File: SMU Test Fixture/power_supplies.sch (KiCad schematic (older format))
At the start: 111 parts, among them J13 Conn_WallSocket_Earth, Q1 Si2347DS, Q10 BC857, Q2 Si2347DS, Q3 BCP56, Q4 Si2347DS, Q5 Si2347DS, Q6 NJVMJB42CT4G, Q7 BCP56, Q8 BCP56, Q9 BCP56, T1 VPP12-4400, T2 VPP36-820, U10 MIC29510-5.0WT, U11 LT3045xMSE-1, U12 LT3094xMSE, U9 LM393

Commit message: Add footprints for low precision/low power parts.
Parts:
- C32, C33: footprint (none) -> Capacitor_SMD:C_0805_2012Metric_Pad1.18x1.45mm_HandSolder
- R31, R32, R33, R34, R35, R36, R37, R38, R39, R40, R66, R67, R68: footprint (none) -> Resistor_SMD:R_0805_2012Metric_Pad1.20x1.40mm_HandSolder
- T1: footprint XFMR_VPP12-4400 -> eaton:XFMR_VPP12-4400
- T2: footprint XFMR_VPP36-820 -> eaton:XFMR_VPP36-820
- U9: footprint (none) -> Package_SO:TSSOP-8_4.4x3mm_P0.65mm
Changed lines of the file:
@@
 F 0 "R66" H 9693 1946 50  0000 L CNN
 F 1 "150k" H 9650 1825 50  0000 L CNN
-F 2 "" H 9625 1900 50  0001 C CNN
+F 2 "Resistor_SMD:R_0805_2012Metric_Pad1.20x1.40mm_HandSolder" H 9625 1900 50  0001 C CNN
 F 3 "~" H 9625 1900 50  0001 C CNN
 	1    9625 1900
@@
 F 0 "R67" H 9693 2546 50  0000 L CNN
 F 1 "150k" H 9650 2425 50  0000 L CNN
-F 2 "" H 9625 2500 50  0001 C CNN
+F 2 "Resistor_SMD:R_0805_2012Metric_Pad1.20x1.40mm_HandSolder" H 9625 2500 50  0001 C CNN
 F 3 "~" H 9625 2500 50  0001 C CNN
 	1    9625 2500
@@
 F 0 "T1" H 2275 6250 50  0000 C CNN
 F 1 "VPP12-4400" H 2275 6150 50  0000 C CNN
-F 2 "XFMR_VPP12-4400" H 2275 5525 50  0001 C CNN
+F 2 "eaton:XFMR_VPP12-4400" H 2275 5525 50  0001 C CNN
 F 3 "https://www.mouser.com/datasheet/2/410/VPP12_4400-781393.pdf" H 2275 5525 50  0001 C CNN
 F 4 "VPP12-4400" H 2275 5525 50  0001 C CNN "PN"
@@
 F 0 "T2" H 5325 2781 50  0000 C CNN
 F 1 "VPP36-820" H 5325 2850 50  0000 C CNN
-F 2 "XFMR_VPP36-820" H 5325 2200 50  0001 C CNN
+F 2 "eaton:XFMR_VPP36-820" H 5325 2200 50  0001 C CNN
 F 3 "https://www.mouser.com/datasheet/2/410/VPP36_820-781788.pdf" H 5325 2200 50  0001 C CNN
 F 4 "VPP36-820" H 5325 2200 50  0001 C CNN "PN"
@@
 F 0 "U9" H 1925 2300 50  0000 C CNN
 F 1 "LM393" H 1875 2225 50  0000 C CNN
-F 2 "" H 1900 2450 50  0001 C CNN
+F 2 "Package_SO:TSSOP-8_4.4x3mm_P0.65mm" H 1900 2450 50  0001 C CNN
 F 3 "http://www.ti.com/lit/ds/symlink/lm393.pdf" H 1900 2450 50  0001 C CNN
 	1    1900 2450
@@
 F 0 "U9" H 1875 3500 50  0000 C CNN
 F 1 "LM393" H 1875 3400 50  0000 C CNN
-F 2 "" H 1875 3750 50  0001 C CNN
+F 2 "Package_SO:TSSOP-8_4.4x3mm_P0.65mm" H 1875 3750 50  0001 C CNN
 F 3 "http://www.ti.com/lit/ds/symlink/lm393.pdf" H 1875 3750 50  0001 C CNN
 	2    1875 3750
@@
 F 0 "R31" H 575 3550 50  0000 L CNN
 F 1 "10k" H 525 3475 50  0000 L CNN
-F 2 "" H 725 3475 50  0001 C CNN
+F 2 "Resistor_SMD:R_0805_2012Metric_Pad1.20x1.40mm_HandSolder" H 725 3475 50  0001 C CNN
 F 3 "~" H 725 3475 50  0001 C CNN
 	1    725  3475
@@
 F 0 "U9" H 1208 1171 50  0000 L CNN
 F 1 "LM393" H 1208 1080 50  0000 L CNN
-F 2 "" H 1250 1125 50  0001 C CNN
+F 2 "Package_SO:TSSOP-8_4.4x3mm_P0.65mm" H 1250 1125 50  0001 C CNN
 F 3 "http://www.ti.com/lit/ds/symlink/lm393.pdf" H 1250 1125 50  0001 C CNN
 	3    1250 1125
@@
 F 0 "R32" H 575 3900 50  0000 L CNN
 F 1 "2.5k" H 500 3800 50  0000 L CNN
-F 2 "" H 725 3825 50  0001 C CNN
+F 2 "Resistor_SMD:R_0805_2012Metric_Pad1.20x1.40mm_HandSolder" H 725 3825 50  0001 C CNN
 F 3 "~" H 725 3825 50  0001 C CNN
 	1    725  3825
@@
 F 0 "C32" H 7875 1675 50  0000 L CNN
 F 1 "1n" H 7925 1600 50  0000 L CNN
-F 2 "" H 7850 1600 50  0001 C CNN
+F 2 "Capacitor_SMD:C_0805_2012Metric_Pad1.18x1.45mm_HandSolder" H 7850 1600 50  0001 C CNN
 F 3 "~" H 7850 1600 50  0001 C CNN
 	1    7850 1600
@@
 F 0 "R39" H 2293 3571 50  0000 L CNN
 F 1 "3K" H 2293 3480 50  0000 L CNN
-F 2 "" H 2225 3525 50  0001 C CNN
+F 2 "Resistor_SMD:R_0805_2012Metric_Pad1.20x1.40mm_HandSolder" H 2225 3525 50  0001 C CNN
 F 3 "~" H 2225 3525 50  0001 C CNN
 	1    2225 3525
@@
 F 0 "R35" V 1475 3850 50  0000 C CNN
 F 1 "10K" V 1550 3850 50  0000 C CNN
-F 2 "" H 1400 3850 50  0001 C CNN
+F 2 "Resistor_SMD:R_0805_2012Metric_Pad1.20x1.40mm_HandSolder" H 1400 3850 50  0001 C CNN
 F 3 "~" H 1400 3850 50  0001 C CNN
 	1    1400 3850
@@
 F 0 "R37" V 2050 4025 50  0000 C CNN
 F 1 "10M" V 1975 4025 50  0000 C CNN
-F 2 "" H 1875 4025 50  0001 C CNN
+F 2 "Resistor_SMD:R_0805_2012Metric_Pad1.20x1.40mm_HandSolder" H 1875 4025 50  0001 C CNN
 F 3 "~" H 1875 4025 50  0001 C CNN
 	1    1875 4025
@@
 F 0 "R33" H 600 2250 50  0000 L CNN
 F 1 "10k" H 550 2175 50  0000 L CNN
-F 2 "" H 750 2175 50  0001 C CNN
+F 2 "Resistor_SMD:R_0805_2012Metric_Pad1.20x1.40mm_HandSolder" H 750 2175 50  0001 C CNN
 F 3 "~" H 750 2175 50  0001 C CNN
 	1    750  2175
@@
 F 0 "R34" H 600 2600 50  0000 L CNN
 F 1 "2.5k" H 525 2500 50  0000 L CNN
-F 2 "" H 750 2525 50  0001 C CNN
+F 2 "Resistor_SMD:R_0805_2012Metric_Pad1.20x1.40mm_HandSolder" H 750 2525 50  0001 C CNN
 F 3 "~" H 750 2525 50  0001 C CNN
 	1    750  2525
@@
 F 0 "R40" H 2318 2271 50  0000 L CNN
 F 1 "3K" H 2318 2180 50  0000 L CNN
-F 2 "" H 2250 2225 50  0001 C CNN
+F 2 "Resistor_SMD:R_0805_2012Metric_Pad1.20x1.40mm_HandSolder" H 2250 2225 50  0001 C CNN
 F 3 "~" H 2250 2225 50  0001 C CNN
 	1    2250 2225
@@
 F 0 "R36" V 1500 2550 50  0000 C CNN
 F 1 "10K" V 1575 2550 50  0000 C CNN
-F 2 "" H 1425 2550 50  0001 C CNN
+F 2 "Resistor_SMD:R_0805_2012Metric_Pad1.20x1.40mm_HandSolder" H 1425 2550 50  0001 C CNN
 F 3 "~" H 1425 2550 50  0001 C CNN
 	1    1425 2550
@@
 F 0 "R38" V 2075 2725 50  0000 C CNN
 F 1 "10M" V 2000 2725 50  0000 C CNN
-F 2 "" H 1900 2725 50  0001 C CNN
+F 2 "Resistor_SMD:R_0805_2012Metric_Pad1.20x1.40mm_HandSolder" H 1900 2725 50  0001 C CNN
 F 3 "~" H 1900 2725 50  0001 C CNN
 	1    1900 2725
@@
 F 0 "C33" H 7875 2875 50  0000 L CNN
 F 1 "1n" H 7925 2800 50  0000 L CNN
-F 2 "" H 7850 2800 50  0001 C CNN
+F 2 "Capacitor_SMD:C_0805_2012Metric_Pad1.18x1.45mm_HandSolder" H 7850 2800 50  0001 C CNN
 F 3 "~" H 7850 2800 50  0001 C CNN
 	1    7850 2800
@@
 F 0 "R68" H 10343 4871 50  0000 L CNN
 F 1 "390K" H 10343 4780 50  0000 L CNN
-F 2 "" H 10275 4825 50  0001 C CNN
+F 2 "Resistor_SMD:R_0805_2012Metric_Pad1.20x1.40mm_HandSolder" H 10275 4825 50  0001 C CNN
 F 3 "~" H 10275 4825 50  0001 C CNN
 	1    10275 4825

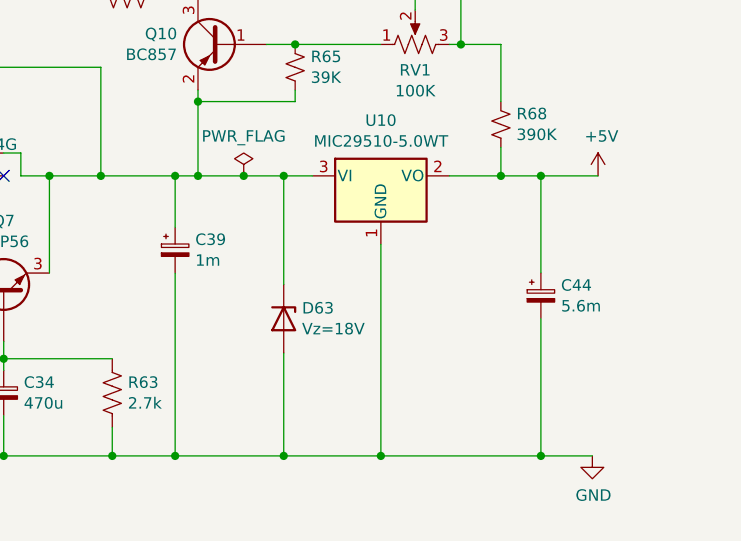
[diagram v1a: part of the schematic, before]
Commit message: More footprints added.
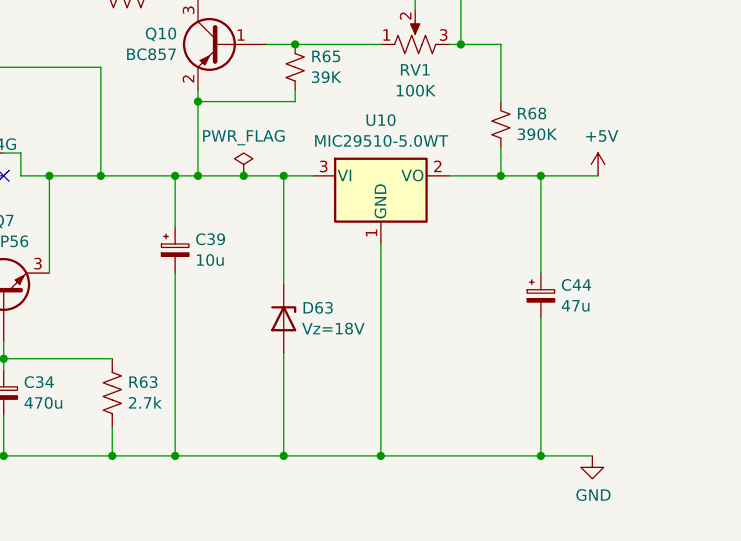
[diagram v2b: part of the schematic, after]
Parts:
- C26, C27, C28, C40, C41, C42, C43, C45, C46: footprint (none) -> Capacitor_SMD:C_0805_2012Metric_Pad1.18x1.45mm_HandSolder
- C39: value 1m -> 10u; footprint Capacitor_SMD:CP_Elec_16x22 -> Capacitor_SMD:C_Elec_5x5.8; PN UCZ1H102MNS1MS -> UUT1V100MCL1GS
- C44: value 5.6m -> 47u; footprint (none) -> Capacitor_SMD:CP_Elec_8x10; PN (none) -> UUB1V470MNL1GS
- D37, D38, D39, D40, D50, D51, D52, D53: footprint (none) -> Package_TO_SOT_SMD:TO-263-3_TabPin2; PN (none) -> VS-8ETH06-1HM3
- D41, D42, D47, D48, D49: footprint (none) -> Diode_SMD:D_SOD-123; PN (none) -> RS07D-HM3-08
- D43, D56, D57: footprint (none) -> Package_TO_SOT_SMD:SOT-323_SC-70_Handsoldering; PN (none) -> SZMMBZH15VAWT1G
- D44, D54, D55: footprint (none) -> Package_TO_SOT_SMD:SOT-323_SC-70_Handsoldering
- D45: footprint (none) -> Diode_SMD:D_SOD-323_HandSoldering; PN (none) -> MM3Z5V6B
- D46: footprint (none) -> Diode_SMD:D_SOD-123
- RV1: footprint (none) -> Potentiometer_SMD:Potentiometer_Bourns_TC33X_Vertical; PN (none) -> TC33X-2-104E

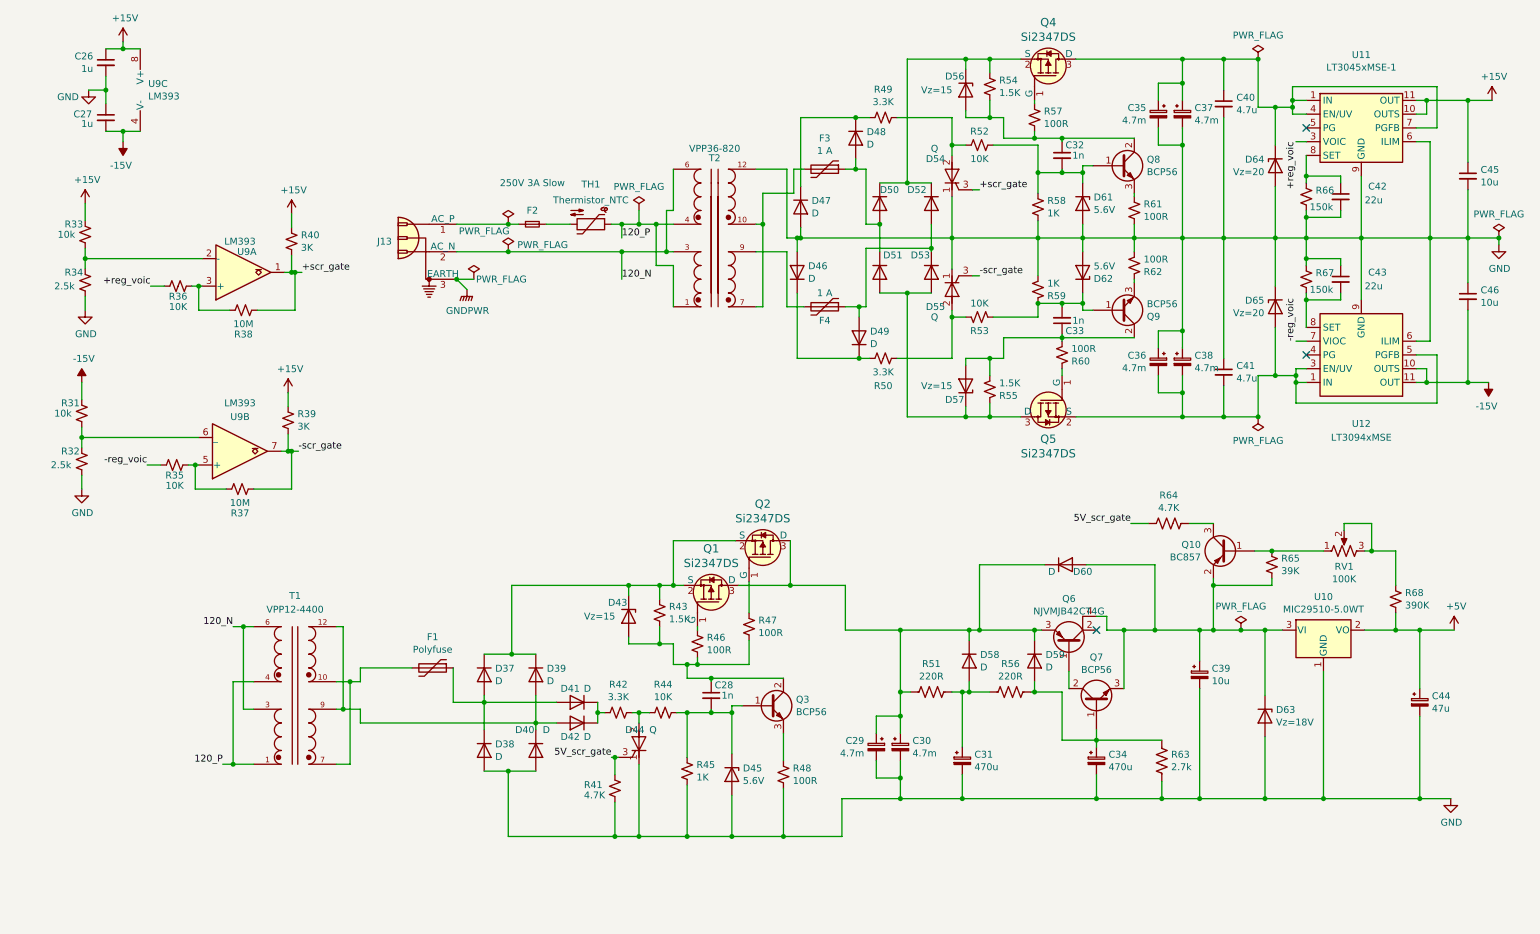
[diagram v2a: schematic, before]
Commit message: NTC calulations/specs done.
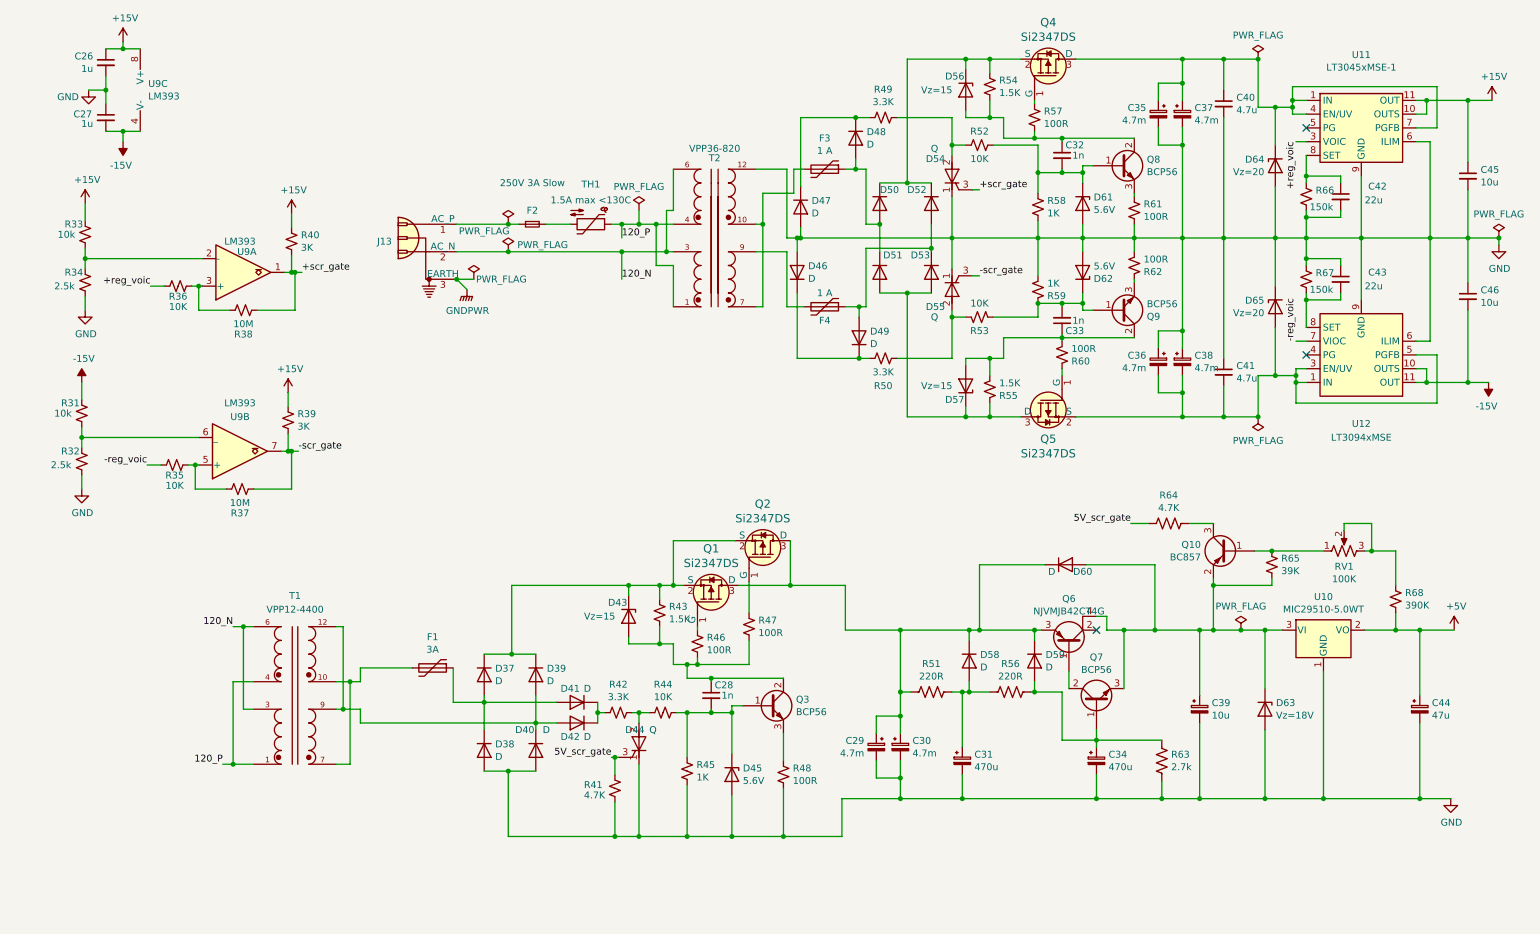
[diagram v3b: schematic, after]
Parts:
- D58, D59, D60: footprint (none) -> Diode_SMD:D_SOD-123; PN (none) -> RS07D-HM3-08
- D61, D62: footprint (none) -> Capacitor_SMD:C_0805_2012Metric_Pad1.18x1.45mm_HandSolder; PN (none) -> BZY55B5V6 RBG
- D63: footprint (none) -> Diode_SMD:D_SOD-523; PN (none) -> BZX584C18-G3-08
- D64, D65: footprint (none) -> Diode_SMD:D_SOD-523; PN (none) -> BZX584C20-G3-08
- F1: value Polyfuse -> 3A; footprint (none) -> Fuse:Fuse_1812_4532Metric_Pad1.30x3.40mm_HandSolder; PN (none) -> MF-MSMF150/24X-2
- R41, R42, R43, R44, R45, R46, R47, R48, R49, R50, R51, R52, R53, R54, R55, R56, R57, R58, R59, R60, R61, R62, R63, R64, R65: footprint (none) -> Resistor_SMD:R_0805_2012Metric_Pad1.20x1.40mm_HandSolder
- TH1: value Thermistor_NTC -> 1.5A max <130C; footprint (none) -> eaton:NTC d=11.5 p=5mm w=6mm; PN (none) -> B57236S0121M051
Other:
- moved on the sheet: C39, C44, D63

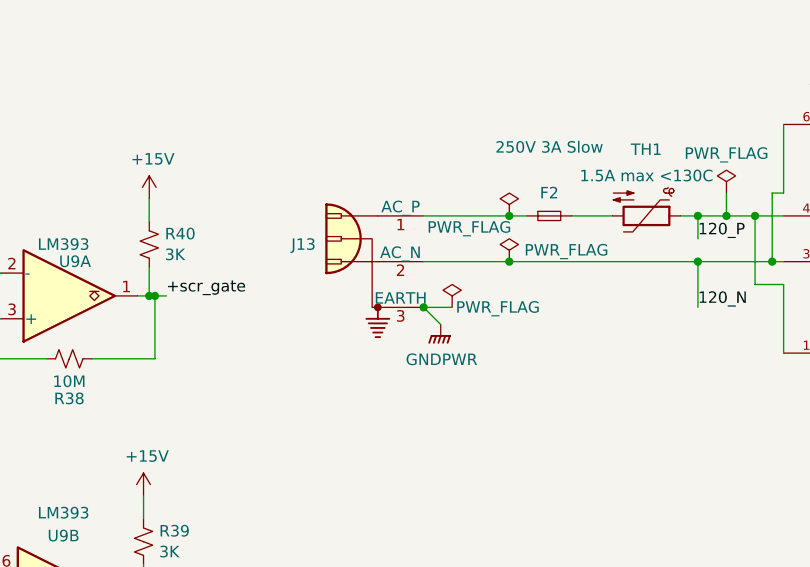
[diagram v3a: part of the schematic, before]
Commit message: Remove edison plug from schematic, now wire holes.
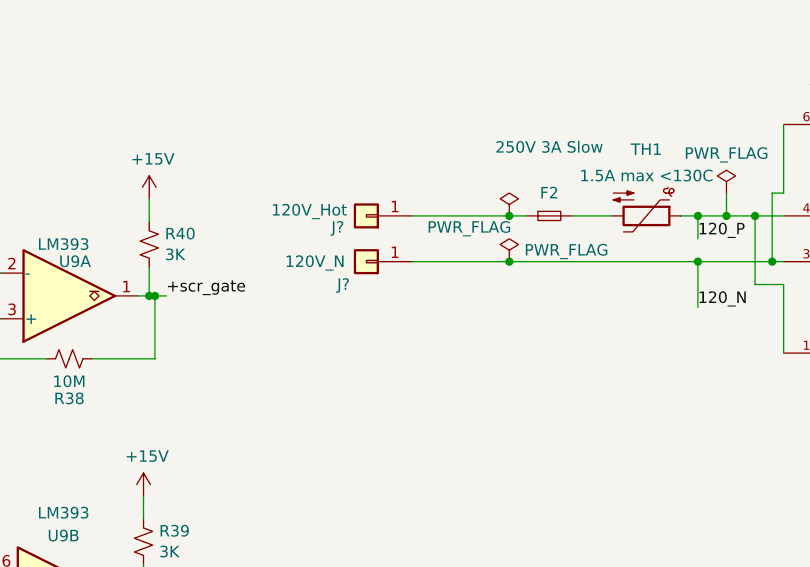
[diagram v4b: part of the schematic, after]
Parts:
- removed J13: Conn_WallSocket_Earth, symbol Connector:Conn_WallSocket_Earth
- added J?: 120V_Hot, Connector_Wire:SolderWire-0.75sqmm_1x01_D1.25mm_OD2.3mm, symbol Connector_Generic:Conn_01x01
- added J?: 120V_N, Connector_Wire:SolderWire-0.75sqmm_1x01_D1.25mm_OD2.3mm, symbol Connector_Generic:Conn_01x01
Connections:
- net 120_N: now also J?.1 (Pin_1)
- net at F2.1: now also J?.1 (Pin_1)
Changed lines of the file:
@@
-$EndComp
-$Comp
-L Connector:Conn_WallSocket_Earth J13
-U 1 1 6010B62B
-P 3250 2300
-F 0 "J13" H 3575 2375 50  0000 C CNN
-F 1 "Conn_WallSocket_Earth" H 3256 2634 50  0001 C CNN
-F 2 "" H 2950 2400 50  0001 C CNN
-F 3 "~" H 2950 2400 50  0001 C CNN
-	1    3250 2300
-	-1   0    0    -1
 $EndComp
 $Comp
@@
 $EndComp
 Wire Wire Line
-	3450 2300 3825 2300
+	3400 2300 3825 2300
 $Comp
 L power:GND #PWR074
@@
 Wire Wire Line
 	9150 5050 9325 5050
-$Comp
-L power:GNDPWR #PWR069
-U 1 1 60086BE8
-P 3525 2575
-F 0 "#PWR069" H 3525 2375 50  0001 C CNN
-F 1 "GNDPWR" H 3529 2421 50  0000 C CNN
-F 2 "" H 3525 2525 50  0001 C CNN
-F 3 "" H 3525 2525 50  0001 C CNN
-	1    3525 2575
-	1    0    0    -1
-$EndComp
-Wire Wire Line
-	3525 2575 3450 2500
-$Comp
-L power:PWR_FLAG #FLG01
-U 1 1 600A3F9C
-P 3575 2500
-F 0 "#FLG01" H 3575 2575 50  0001 C CNN
-F 1 "PWR_FLAG" H 3775 2500 50  0000 C CNN
-F 2 "" H 3575 2500 50  0001 C CNN
-F 3 "~" H 3575 2500 50  0001 C CNN
-	1    3575 2500
-	1    0    0    -1
-$EndComp
-Wire Wire Line
-	3575 2500 3450 2500
-Connection ~ 3450 2500
-Wire Wire Line
-	3450 2100 3825 2100
+Wire Wire Line
+	3400 2100 3825 2100
 $Comp
 L power:PWR_FLAG #FLG04
@@
 	0    1    1    0
 $EndComp
+$Comp
+L Connector_Generic:Conn_01x01 J?
+U 1 1 601511D3
+P 3200 2100
+F 0 "J?" H 3325 2150 50  0000 C CNN
+F 1 "120V_Hot" H 3450 2075 50  0000 C CNN
+F 2 "Connector_Wire:SolderWire-0.75sqmm_1x01_D1.25mm_OD2.3mm" H 3200 2100 50  0001 C CNN
+F 3 "~" H 3200 2100 50  0001 C CNN
+	1    3200 2100
+	-1   0    0    1
+$EndComp
+$Comp
+L Connector_Generic:Conn_01x01 J?
+U 1 1 60151E3B
+P 3200 2300
+F 0 "J?" H 3300 2400 50  0000 C CNN
+F 1 "120V_N" H 3425 2300 50  0000 C CNN
+F 2 "Connector_Wire:SolderWire-0.75sqmm_1x01_D1.25mm_OD2.3mm" H 3200 2300 50  0001 C CNN
+F 3 "~" H 3200 2300 50  0001 C CNN
+	1    3200 2300
+	-1   0    0    1
+$EndComp
 $EndSCHEMATC
